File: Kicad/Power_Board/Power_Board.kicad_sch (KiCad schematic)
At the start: 17 parts, among them J1 Conn_01x04_Pin, U1 PTPS543021DRLR, U2 PTPS543021DRLR

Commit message: Updated schematic for main board
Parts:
- C4: value 33u -> 44u
- L1: value 10uH -> 6.8uH
- R5: value 13.3k -> 22.1k
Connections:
- net 3v3 Output: now reaches C4.1, C5.1, J1.4 (Pin_4), L1.2, R4.1
- net 12v Output: now reaches C7.1, C8.1, J1.1 (Pin_1), L2.2, R7.1
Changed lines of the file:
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@@
+		)
+	)
+	(label "3v3 Output"
+		(at 214.63 46.99 0)
+		(effects
+			(font
+				(size 1.27 1.27)
+			)
+			(justify left bottom)
 		)
 	)
@@
 		)
 	)
+	(label "12v Output"
+		(at 210.82 105.41 0)
+		(effects
+			(font
+				(size 1.27 1.27)
+			)
+			(justify left bottom)
+		)
+	)
 	(symbol
 		(lib_id "Device:R")
@@
 			)
 		)
-		(property "Value" "13.3k"
+		(property "Value" "22.1k"
 			(at 198.12 72.3899 0)
 			(effects
@@
 			)
 		)
-		(property "Value" "10uH"
+		(property "Value" "6.8uH"
 			(at 166.37 44.45 90)
 			(effects
@@
 			)
 		)
-		(property "Value" "33u"
+		(property "Value" "44u"
 			(at 180.34 54.6099 0)
 			(effects

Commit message: Main Board v1
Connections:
- net Boot: now reaches C3.1, U1.6 (BOOT)
- net SW: now reaches C3.2, L1.1, U1.2 (SW)
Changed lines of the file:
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@@
+		)
+	)
+	(label "Boot"
+		(at 146.05 39.37 0)
+		(effects
+			(font
+				(size 1.27 1.27)
+			)
+			(justify left bottom)
 		)
 	)
@@
 		(effects
 			(font
+				(size 1.27 1.27)
+			)
+			(justify left bottom)
+		)
+	)
+	(label "SW"
+		(at 146.05 46.99 0)
+		(effects
+			(font

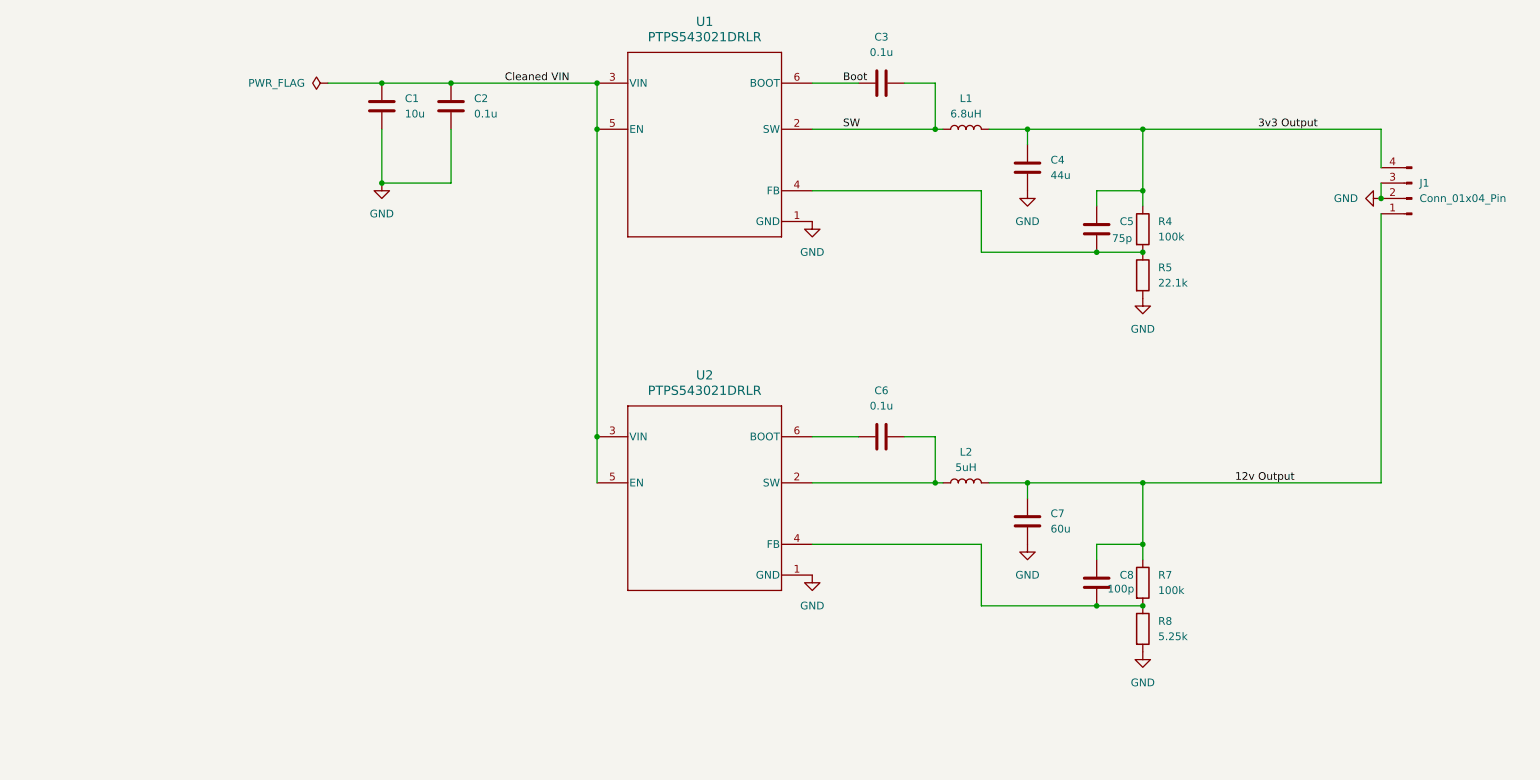
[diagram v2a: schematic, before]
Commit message: Created cad for how the boards will fit together
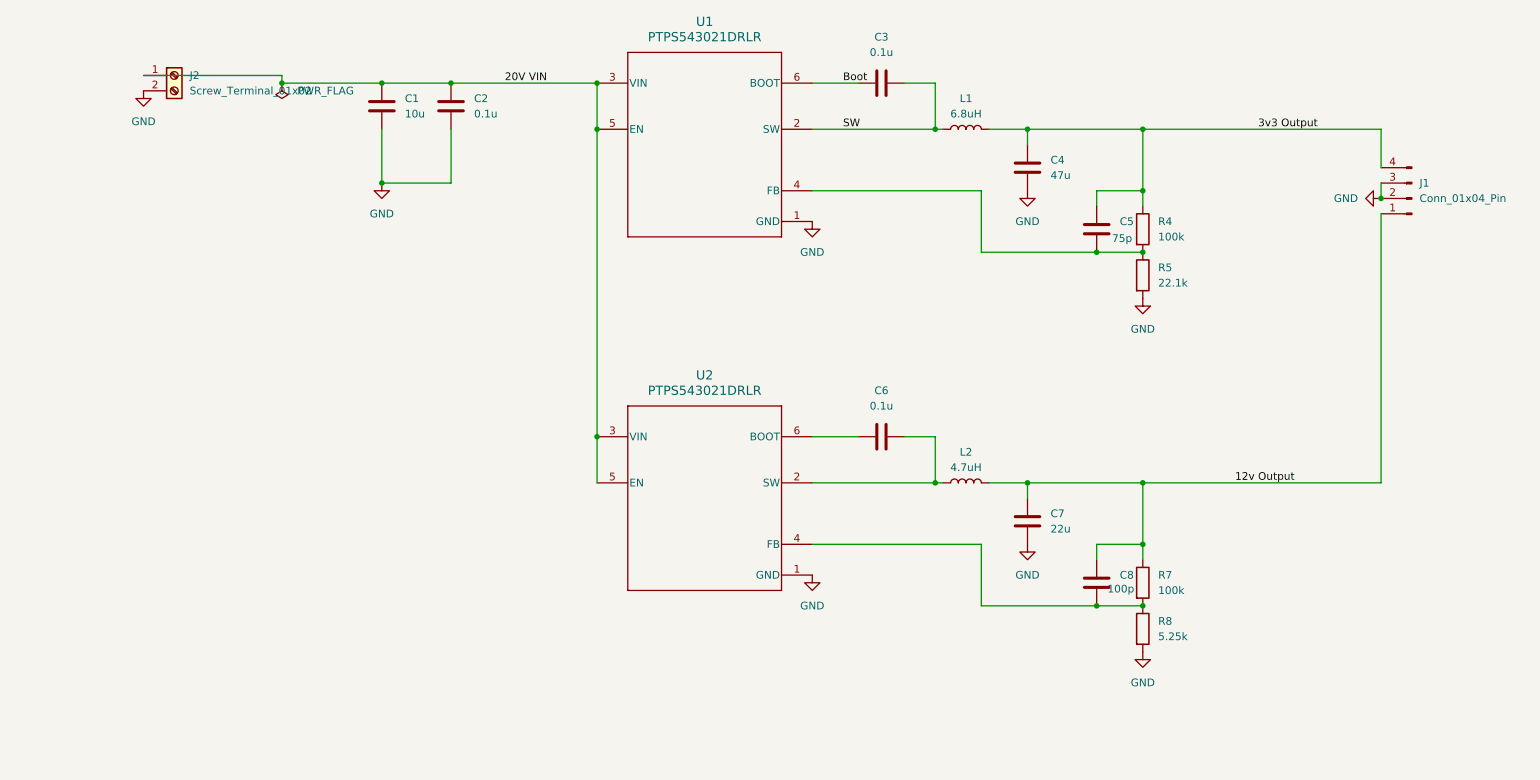
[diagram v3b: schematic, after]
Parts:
- added J2: Screw_Terminal_01x02, TerminalBlock_RND:TerminalBlock_RND_205-00045_1x02_P5.00mm_Horizontal, symbol Connector:Screw_Terminal_01x02
- C4: value 44u -> 47u
- C7: value 60u -> 22u
- J1: footprint Connector_PinHeader_2.54mm:PinHeader_1x04_P2.54mm_Vertical -> Connector_PinSocket_2.54mm:PinSocket_1x04_P2.54mm_Vertical
- L2: value 5uH -> 4.7uH
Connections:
- net GND: now also J2.2 (Pin_2)
- net Cleaned VIN renamed 20V VIN
- net 20V VIN: now also J2.1 (Pin_1)
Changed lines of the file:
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@@
+	)
+	(junction
+		(at 53.34 39.37)
+		(diameter 0)
+		(color 0 0 0 0)
 	)
 	(junction
@@
 	(wire
 		(pts
-			(xy 69.85 39.37) (xy 60.96 39.37)
+			(xy 69.85 39.37) (xy 53.34 39.37)
 		)
 		(stroke
@@
 	(wire
 		(pts
+			(xy 53.34 38.1) (xy 53.34 39.37)
+		)
+		(stroke
+			(width 0)
+			(type default)
+		)
+	)
+	(wire
+		(pts
 			(xy 195.58 105.41) (xy 195.58 115.57)
 		)
@@
 		(pts
 			(xy 140.97 46.99) (xy 161.29 46.99)
+		)
+		(stroke
+			(width 0)
+			(type default)
+		)
+	)
+	(wire
+		(pts
+			(xy 30.48 38.1) (xy 53.34 38.1)
 		)
 		(stroke
@@
 		)
 	)
-	(label "Cleaned VIN"
+	(label "20V VIN"
 		(at 90.17 39.37 0)
 		(effects
@@
 	)
 	(symbol
+		(lib_id "power:GND")
+		(at 30.48 40.64 0)
+		(unit 1)
+		(exclude_from_sim no)
+		(in_bom yes)
+		(on_board yes)
+		(dnp no)
+		(fields_autoplaced yes)
+		(property "Reference" "#PWR09"
+			(at 30.48 46.99 0)
+			(effects
+				(font
+					(size 1.27 1.27)
+				)
+				(hide yes)
+			)
+		)
+		(property "Value" "GND"
+			(at 30.48 45.72 0)
+			(effects
+				(font
+					(size 1.27 1.27)
+				)
+			)
+		)
+		(property "Footprint" ""
+			(at 30.48 40.64 0)
+			(effects
+				(font
+					(size 1.27 1.27)
+				)
+				(hide yes)
+			)
+		)
+		(property "Datasheet" ""
+			(at 30.48 40.64 0)
+			(effects
+				(font
+					(size 1.27 1.27)
+				)
+				(hide yes)
+			)
+		)
+		(property "Description" "Power symbol creates a global label with name \"GND\" , ground"
+			(at 30.48 40.64 0)
+			(effects
+				(font
+					(size 1.27 1.27)
+				)
+				(hide yes)
+			)
+		)
+		(pin "1"
+		)
+		(instances
+			(project ""
+				(path "/58e41d84-7531-48ee-9ca8-bd5b3cfb53b6"
+					(reference "#PWR09")
+					(unit 1)
+				)
+			)
+		)
+	)
+	(symbol
 		(lib_id "Device:C")
 		(at 187.96 121.92 0)
@@
 			)
 		)
-		(property "Footprint" "Connector_PinHeader_2.54mm:PinHeader_1x04_P2.54mm_Vertical"
+		(property "Footprint" "Connector_PinSocket_2.54mm:PinSocket_1x04_P2.54mm_Vertical"
 			(at 240.03 58.42 0)
 			(effects
@@
 			)
 		)
-		(property "Value" "60u"
+		(property "Value" "22u"
 			(at 180.34 113.0299 0)
 			(effects
@@
 	)
 	(symbol
+		(lib_id "Connector:Screw_Terminal_01x02")
+		(at 35.56 38.1 0)
+		(unit 1)
+		(exclude_from_sim no)
+		(in_bom yes)
+		(on_board yes)
+		(dnp no)
+		(fields_autoplaced yes)
+		(property "Reference" "J2"
+			(at 38.1 38.0999 0)
+			(effects
+				(font
+					(size 1.27 1.27)
+				)
+				(justify left)
+			)
+		)
+		(property "Value" "Screw_Terminal_01x02"
+			(at 38.1 40.6399 0)
+			(effects
+				(font
+					(size 1.27 1.27)
+				)
+				(justify left)
+			)
+		)
+		(property "Footprint" "TerminalBlock_RND:TerminalBlock_RND_205-00045_1x02_P5.00mm_Horizontal"
+			(at 35.56 38.1 0)
+			(effects
+				(font
+					(size 1.27 1.27)
+				)
+				(hide yes)
+			)
+		)
+		(property "Datasheet" "~"
+			(at 35.56 38.1 0)
+			(effects
+				(font
+					(size 1.27 1.27)
+				)
+				(hide yes)
+			)
+		)
+		(property "Description" "Generic screw terminal, single row, 01x02, script generated (kicad-library-utils/schlib/autogen/connector/)"
+			(at 35.56 38.1 0)
+			(effects
+				(font
+					(size 1.27 1.27)
+				)
+				(hide yes)
+			)
+		)
+		(pin "1"
+		)
+		(pin "2"
+		)
+		(instances
+			(project ""
+				(path "/58e41d84-7531-48ee-9ca8-bd5b3cfb53b6"
+					(reference "J2")
+					(unit 1)
+				)
+			)
+		)
+	)
+	(symbol
 		(lib_id "Device:C")
 		(at 81.28 43.18 0)
@@
 	(symbol
 		(lib_id "power:PWR_FLAG")
-		(at 60.96 39.37 90)
+		(at 53.34 39.37 180)
 		(unit 1)
 		(exclude_from_sim no)
@@
 		(fields_autoplaced yes)
 		(property "Reference" "#FLG01"
-			(at 59.055 39.37 0)
+			(at 53.34 41.275 0)
 			(effects
 				(font
@@
 		)
 		(property "Value" "PWR_FLAG"
-			(at 57.15 39.3699 90)
-			(effects
-				(font
-					(size 1.27 1.27)
-				)
-				(justify left)
+			(at 55.88 40.6399 0)
+			(effects
+				(font
+					(size 1.27 1.27)
+				)
+				(justify right)
 			)
 		)
 		(property "Footprint" ""
-			(at 60.96 39.37 0)
+			(at 53.34 39.37 0)
 			(effects
 				(font
@@
 		)
 		(property "Datasheet" "~"
-			(at 60.96 39.37 0)
+			(at 53.34 39.37 0)
 			(effects
 				(font
@@
 		)
 		(property "Description" "Special symbol for telling ERC where power comes from"
-			(at 60.96 39.37 0)
+			(at 53.34 39.37 0)
 			(effects
 				(font
@@
 			)
 		)
-		(property "Value" "5uH"
+		(property "Value" "4.7uH"
 			(at 166.37 102.87 90)
 			(effects
@@
 			)
 		)
-		(property "Value" "44u"
+		(property "Value" "47u"
 			(at 180.34 54.6099 0)
 			(effects

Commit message: Wrote v1 of the code, final version of boards
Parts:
- C1: value 10u -> 10uF; footprint Capacitor_SMD:C_0603_1608Metric -> PCM_JLCPCB:C_0603; symbol Device:C -> PCM_JLCPCB-Capacitors:0603,10uF,(2); Attrition Qty (none) -> 8; Capacitance (none) -> 10uF; Category (none) -> Capacitors,Multilayer Ceramic Capacitors MLCC - SMD/SMT; Class (none) -> Basic Component; LCSC (none) -> C96446; Manufacturer (none) -> Samsung Electro-Mechanics; Minimum Qty (none) -> 20; Part (none) -> CL10A106MA8NRNC; Price (none) -> 0.021USD; Process (none) -> SMT; Stock (none) -> 3388297; Temperature Coefficient (none) -> X5R; Tolerance (none) -> ±20%; Voltage Rated (none) -> 25V
- C2, C3, C6: value 0.1u -> 100nF; footprint Capacitor_SMD:C_0603_1608Metric -> PCM_JLCPCB:C_0603; symbol Device:C -> PCM_JLCPCB-Capacitors:0603,100nF; Attrition Qty (none) -> 10; Capacitance (none) -> 100nF; Category (none) -> Capacitors,Multilayer Ceramic Capacitors MLCC - SMD/SMT; Class (none) -> Basic Component; LCSC (none) -> C14663; Manufacturer (none) -> YAGEO; Minimum Qty (none) -> 20; Part (none) -> CC0603KRX7R9BB104; Price (none) -> 0.006USD; Process (none) -> SMT; Stock (none) -> 70324515; Temperature Coefficient (none) -> X7R; Tolerance (none) -> ±10%; Voltage Rated (none) -> 50V
- C4: value 47u -> 47uF; footprint Capacitor_SMD:C_0603_1608Metric -> PCM_JLCPCB:C_0805; symbol Device:C -> PCM_JLCPCB-Capacitors:0805,47uF; Attrition Qty (none) -> 6; Capacitance (none) -> 47uF; Category (none) -> Capacitors,Multilayer Ceramic Capacitors MLCC - SMD/SMT; Class (none) -> Basic Component; LCSC (none) -> C16780; Manufacturer (none) -> Samsung Electro-Mechanics; Minimum Qty (none) -> 5; Part (none) -> CL21A476MQYNNNE; Price (none) -> 0.030USD; Process (none) -> SMT; Stock (none) -> 1584628; Temperature Coefficient (none) -> X5R; Tolerance (none) -> ±20%; Voltage Rated (none) -> 6.3V
- C5: value 75p -> 68pF; footprint Capacitor_SMD:C_0603_1608Metric -> PCM_JLCPCB:C_0603; symbol Device:C -> PCM_JLCPCB-Capacitors:0603,68pF; Attrition Qty (none) -> 10; Capacitance (none) -> 68pF; Category (none) -> Capacitors,Multilayer Ceramic Capacitors MLCC - SMD/SMT; Class (none) -> Preferred Component; LCSC (none) -> C28262; Manufacturer (none) -> Samsung Electro-Mechanics; Minimum Qty (none) -> 20; Part (none) -> CL10C680JB8NNNC; Price (none) -> 0.007USD; Process (none) -> SMT; Stock (none) -> 80166; Temperature Coefficient (none) -> C0G; Tolerance (none) -> ±5%; Voltage Rated (none) -> 50V
- C7: value 22u -> 22uF; footprint Capacitor_SMD:C_0603_1608Metric -> PCM_JLCPCB:C_0805; symbol Device:C -> PCM_JLCPCB-Capacitors:0805,22uF; Attrition Qty (none) -> 8; Capacitance (none) -> 22uF; Category (none) -> Capacitors,Multilayer Ceramic Capacitors MLCC - SMD/SMT; Class (none) -> Basic Component; LCSC (none) -> C45783; Manufacturer (none) -> Samsung Electro-Mechanics; Minimum Qty (none) -> 20; Part (none) -> CL21A226MAQNNNE; Price (none) -> 0.027USD; Process (none) -> SMT; Stock (none) -> 6479946; Temperature Coefficient (none) -> X5R; Tolerance (none) -> ±20%; Voltage Rated (none) -> 25V
- C8: value 100p -> 100pF; footprint Capacitor_SMD:C_0603_1608Metric -> PCM_JLCPCB:C_0603; symbol Device:C -> PCM_JLCPCB-Capacitors:0603,100pF; Attrition Qty (none) -> 10; Capacitance (none) -> 100pF; Category (none) -> Capacitors,Multilayer Ceramic Capacitors MLCC - SMD/SMT; Class (none) -> Basic Component; LCSC (none) -> C14858; Manufacturer (none) -> Samsung Electro-Mechanics; Minimum Qty (none) -> 20; Part (none) -> CL10C101JB8NNNC; Price (none) -> 0.007USD; Process (none) -> SMT; Stock (none) -> 2210509; Temperature Coefficient (none) -> C0G; Tolerance (none) -> ±5%; Voltage Rated (none) -> 50V
- L1, L2: footprint Inductor_SMD:L_0603_1608Metric -> Inductor_SMD:L_TDK_VLS6045EX_VLS6045AF
- R4, R7: value 100k -> 100kΩ; footprint Resistor_SMD:R_0603_1608Metric -> PCM_JLCPCB:R_0603; symbol Device:R -> PCM_JLCPCB-Resistors:0603,100kΩ; Attrition Qty (none) -> 10; Category (none) -> Resistors,Chip Resistor - Surface Mount; Class (none) -> Basic Component; LCSC (none) -> C25803; Manufacturer (none) -> UNI-ROYAL(Uniroyal Elec); Minimum Qty (none) -> 20; Operating Temperature Range (none) -> -55°C~+155°C; Overload Voltage (Max) (none) -> 75V; Part (none) -> 0603WAF1003T5E; Power(Watts) (none) -> 100mW; Price (none) -> 0.004USD; Process (none) -> SMT; Resistance (none) -> 100kΩ; Stock (none) -> 7820113; Temperature Coefficient (none) -> ±100ppm/°C; Tolerance (none) -> ±1%; Type (none) -> Thick Film Resistors
- R5: value 22.1k -> 22kΩ; footprint Resistor_SMD:R_0603_1608Metric -> PCM_JLCPCB:R_0603; symbol Device:R -> PCM_JLCPCB-Resistors:0603,22kΩ; Attrition Qty (none) -> 10; Category (none) -> Resistors,Chip Resistor - Surface Mount; Class (none) -> Basic Component; LCSC (none) -> C31850; Manufacturer (none) -> UNI-ROYAL(Uniroyal Elec); Minimum Qty (none) -> 20; Operating Temperature Range (none) -> -55°C~+155°C; Overload Voltage (Max) (none) -> 75V; Part (none) -> 0603WAF2202T5E; Power(Watts) (none) -> 100mW; Price (none) -> 0.004USD; Process (none) -> SMT; Resistance (none) -> 22kΩ; Stock (none) -> 1601895; Temperature Coefficient (none) -> ±100ppm/°C; Tolerance (none) -> ±1%; Type (none) -> Thick Film Resistors
- R8: value 5.25k -> 5.1kΩ; footprint Resistor_SMD:R_0603_1608Metric -> PCM_JLCPCB:R_0603; symbol Device:R -> PCM_JLCPCB-Resistors:0603,5.1kΩ; Attrition Qty (none) -> 10; Category (none) -> Resistors,Chip Resistor - Surface Mount; Class (none) -> Basic Component; LCSC (none) -> C23186; Manufacturer (none) -> UNI-ROYAL(Uniroyal Elec); Minimum Qty (none) -> 20; Operating Temperature Range (none) -> -55°C~+155°C; Overload Voltage (Max) (none) -> 75V; Part (none) -> 0603WAF5101T5E; Power(Watts) (none) -> 100mW; Price (none) -> 0.004USD; Process (none) -> SMT; Resistance (none) -> 5.1kΩ; Stock (none) -> 9223405; Temperature Coefficient (none) -> ±100ppm/°C; Tolerance (none) -> ±1%; Type (none) -> Thick Film Resistors
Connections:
- net FB: now reaches C5.2, R4.2, R5.1, U1.4 (FB)
- net FB 12V: now reaches C8.2, R7.2, R8.1, U2.4 (FB)
- net SW 12V: now reaches C6.2, L2.1, U2.2 (SW)
- net BOOT 12V: now reaches C6.1, U2.6 (BOOT)
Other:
- moved on the sheet: C1, J2

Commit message: Updated to use 0805 instead of JLC assembly
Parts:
- C1, C2, C3, C5, C6, C8: footprint PCM_JLCPCB:C_0603 -> Capacitor_SMD:C_0805_2012Metric_Pad1.18x1.45mm_HandSolder
- C4, C7: footprint PCM_JLCPCB:C_0805 -> Capacitor_SMD:C_0805_2012Metric_Pad1.18x1.45mm_HandSolder
- R4, R5, R7, R8: footprint PCM_JLCPCB:R_0603 -> Resistor_SMD:R_0805_2012Metric_Pad1.20x1.40mm_HandSolder
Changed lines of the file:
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@@
 			)
 		)
-		(property "Footprint" "PCM_JLCPCB:R_0603"
+		(property "Footprint" "Resistor_SMD:R_0805_2012Metric_Pad1.20x1.40mm_HandSolder"
 			(at 193.802 63.5 90)
 			(effects
@@
 			)
 		)
-		(property "Footprint" "PCM_JLCPCB:R_0603"
+		(property "Footprint" "Resistor_SMD:R_0805_2012Metric_Pad1.20x1.40mm_HandSolder"
 			(at 193.802 129.54 90)
 			(effects
@@
 			)
 		)
-		(property "Footprint" "PCM_JLCPCB:C_0603"
+		(property "Footprint" "Capacitor_SMD:C_0805_2012Metric_Pad1.18x1.45mm_HandSolder"
 			(at 186.182 121.92 90)
 			(effects
@@
 			)
 		)
-		(property "Footprint" "PCM_JLCPCB:R_0603"
+		(property "Footprint" "Resistor_SMD:R_0805_2012Metric_Pad1.20x1.40mm_HandSolder"
 			(at 193.802 121.92 90)
 			(effects
@@
 			)
 		)
-		(property "Footprint" "PCM_JLCPCB:C_0603"
+		(property "Footprint" "Capacitor_SMD:C_0805_2012Metric_Pad1.18x1.45mm_HandSolder"
 			(at 152.4 41.148 90)
 			(effects
@@
 			)
 		)
-		(property "Footprint" "PCM_JLCPCB:C_0603"
+		(property "Footprint" "Capacitor_SMD:C_0805_2012Metric_Pad1.18x1.45mm_HandSolder"
 			(at 68.072 46.99 90)
 			(effects
@@
 			)
 		)
-		(property "Footprint" "PCM_JLCPCB:C_0805"
+		(property "Footprint" "Capacitor_SMD:C_0805_2012Metric_Pad1.18x1.45mm_HandSolder"
 			(at 174.752 111.76 90)
 			(effects
@@
 			)
 		)
-		(property "Footprint" "PCM_JLCPCB:C_0603"
+		(property "Footprint" "Capacitor_SMD:C_0805_2012Metric_Pad1.18x1.45mm_HandSolder"
 			(at 79.502 43.18 90)
 			(effects
@@
 			)
 		)
-		(property "Footprint" "PCM_JLCPCB:R_0603"
+		(property "Footprint" "Resistor_SMD:R_0805_2012Metric_Pad1.20x1.40mm_HandSolder"
 			(at 193.802 71.12 90)
 			(effects
@@
 			)
 		)
-		(property "Footprint" "PCM_JLCPCB:C_0805"
+		(property "Footprint" "Capacitor_SMD:C_0805_2012Metric_Pad1.18x1.45mm_HandSolder"
 			(at 174.752 53.34 90)
 			(effects
@@
 			)
 		)
-		(property "Footprint" "PCM_JLCPCB:C_0603"
+		(property "Footprint" "Capacitor_SMD:C_0805_2012Metric_Pad1.18x1.45mm_HandSolder"
 			(at 152.4 99.568 90)
 			(effects
@@
 			)
 		)
-		(property "Footprint" "PCM_JLCPCB:C_0603"
+		(property "Footprint" "Capacitor_SMD:C_0805_2012Metric_Pad1.18x1.45mm_HandSolder"
 			(at 186.182 63.5 90)
 			(effects
